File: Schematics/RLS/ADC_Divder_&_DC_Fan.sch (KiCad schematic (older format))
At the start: 11 parts, among them J7 DC_Fan, Q1 BS170

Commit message: Lots of changes
Completed Schematic
1/3 Done PCB
Multisim file for testing ADC protection and buffer circuit
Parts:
- added R34, R35, R36, R37: 10K, Resistors_SMD:R_1206_HandSoldering, symbol R
- added R38, R39: 1K, Resistors_SMD:R_1206_HandSoldering, symbol R
- added U15, U16, U19, U20: RB496EATR, TO_SOT_Packages_SMD:SOT-23-5_HandSoldering, symbol RB496EATR
- added U17, U18, U21: NE5532, Housings_SOIC:SOIC-8_3.9x4.9mm_Pitch1.27mm, symbol NE5532
- R11: value 20K -> 120
- R12: value 10K -> 120
- R13: value 20K -> 1K
- R14: value 10K -> 1K
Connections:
- net AGND: now also R34.1, R37.1, U15.5, U16.3, U18.5 (+), U19.3, U20.5, U21.5 (+); no longer R12.2, R14.2, R16.2
- net VM01: now also R15.2; no longer R15.1
- net VM02: now also R11.2; no longer R13.1
- net VM03: now also R35.2; no longer R11.1
- net FAN_GND: now reaches C45.2, J7.1 (P1), Q1.1 (D)
- net VGS_FAN: now reaches Q1.2 (G), R29.1, TH1.2
- net VD01 renamed +15_DIV
- net +15_DIV: now also R34.2, U17.5 (+); no longer R15.2
- net VD02 renamed -5_BUFF
- net -5_BUFF: now also U18.1, U18.2 (-); no longer R14.1
- net VD03 renamed +5_OVP
- net +5_OVP: now also U16.1, U16.4, U17.3 (+); no longer R11.2
- new net +15V: U17.8 (V+), U17.8 (V+), U18.8 (V+), U18.8 (V+), U19.5, U21.8 (V+), U21.8 (V+)
- new net +15_OVP: R15.1, R16.2, U19.1, U19.4
- new net +5V_R: U16.5
- new net -15V: U17.4 (V-), U17.4 (V-), U18.4 (V-), U18.4 (V-), U20.3, U21.4 (V-), U21.4 (V-)
- new net -15_BUFF: R38.2, U21.1, U21.2 (-)
- new net -15_DIV: R36.1, R37.2, U21.3 (+)
- new net -15_INV: R38.1, R39.2, U21.6 (-)
- new net -15_OVP: R35.1, R36.2, U20.1, U20.4
- new net -5V_R: U15.3
- new net -5_INV: R13.1, R14.2, U18.6 (-)
- new net -5_OVP: R11.1, U15.1, U15.4, U18.3 (+)
- new net AIN0: U17.1, U17.2 (-)
- new net AIN1: U17.6 (-), U17.7
- new net AIN2: R14.1, U18.7
- new net AIN3: R39.1, U21.7
- new net VM00: R12.2
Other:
- note added: "+15V Buffer Circuit"
- note added: "+5V Buffer Circuit"
- note added: "-15V Buffer and Inverting Circuit"
- note added: "-5V Buffer and Inverting Circuit"
- note added: "5V DC Fan with Thermal\nVoltage Control Circuit"
- moved on the sheet: C45, J7, Q1, R29, TH1

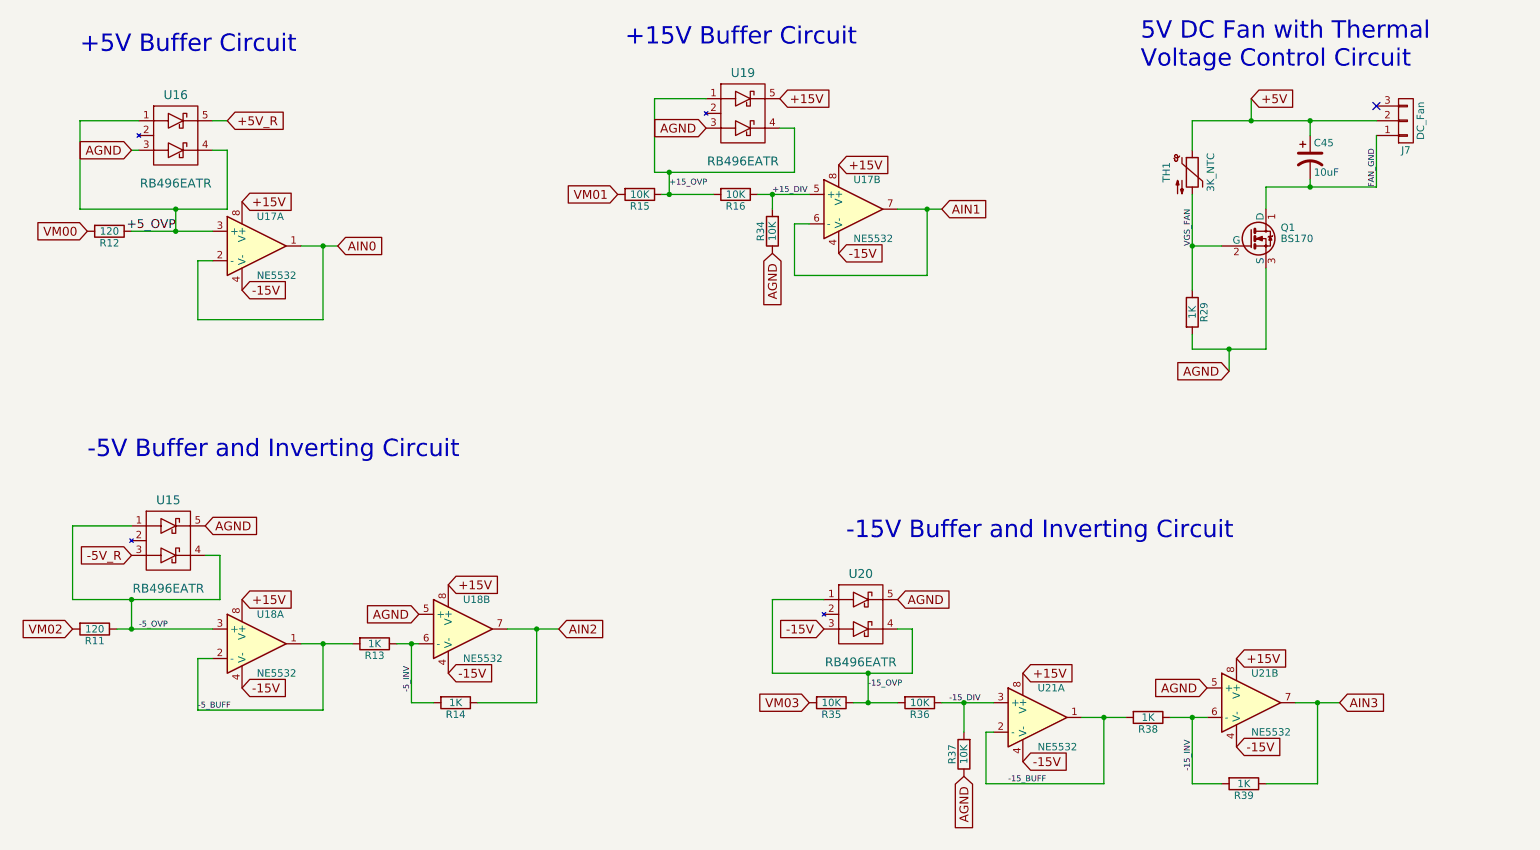
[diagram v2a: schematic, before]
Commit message: Finished PCB but...
Somehow managed to break the schematic file. I know how to fix it, but it is tedious and pointless for now (one has to go through every single individual component and verify that it is the same in the PCB, since the annotation script fucked everything up in the schematic, and therefore any new Netlist).
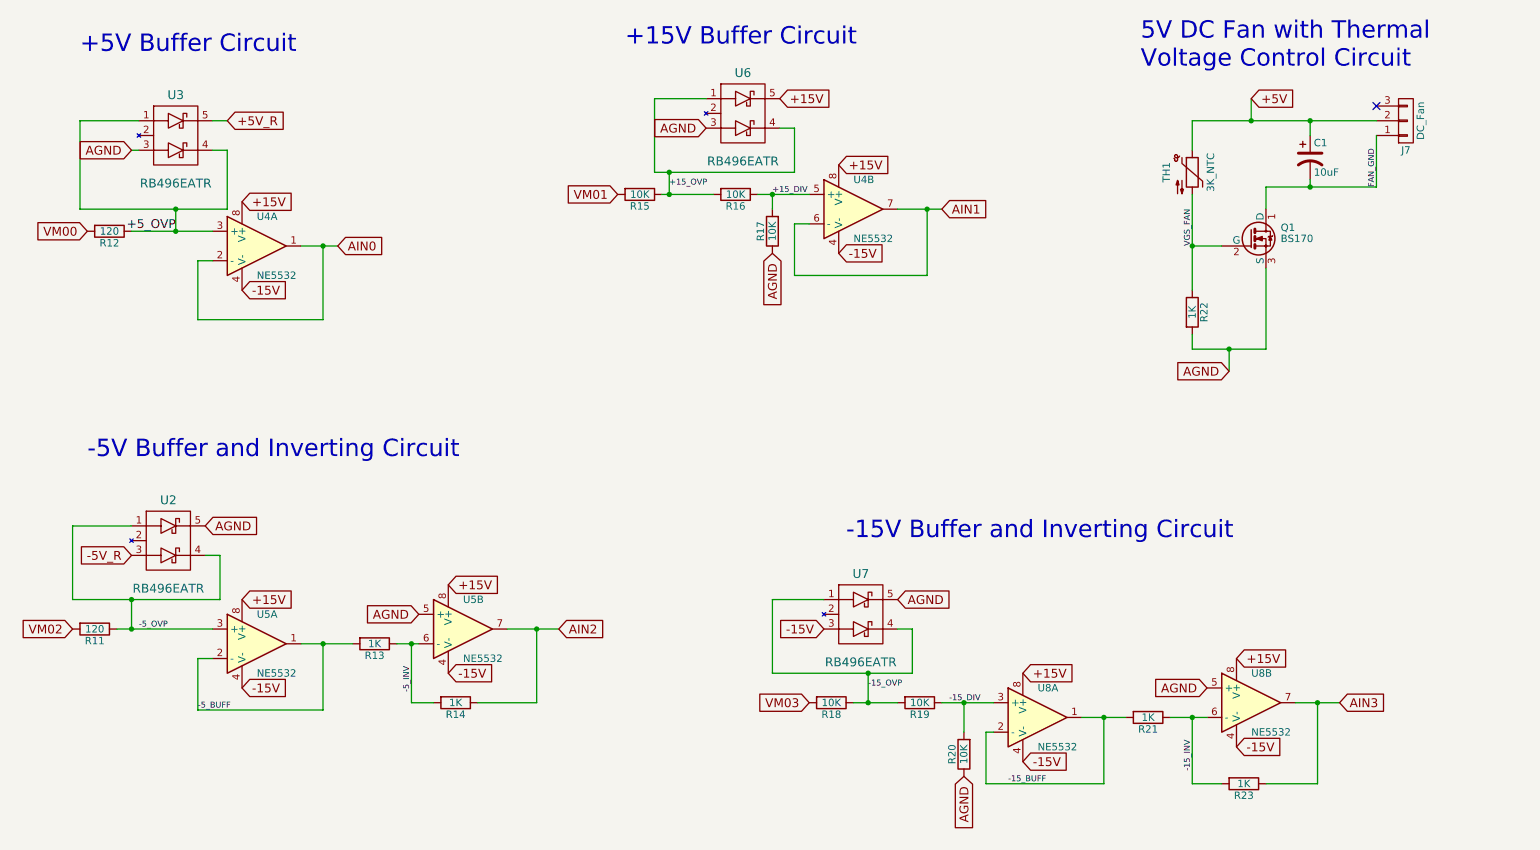
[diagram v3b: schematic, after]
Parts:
- renumbered C45 to C1, R34 to R17, R35 to R18, R36 to R19, R37 to R20, R38 to R21, R29 to R22, R39 to R23, U15 to U2, U16 to U3, U17 to U4, U18 to U5, U19 to U6, U20 to U7, U21 to U8
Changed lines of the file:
@@
 $EndComp
 $Comp
-L R R29
+L R R22
 U 1 1 595B0B7F
 P 8900 2650
-F 0 "R29" V 8980 2650 50  0000 C CNN
+F 0 "R22" V 8980 2650 50  0000 C CNN
 F 1 "1K" V 8900 2650 50  0000 C CNN
 F 2 "Resistors_SMD:R_1206_HandSoldering" V 8830 2650 50  0001 C CNN
@@
 $EndComp
 $Comp
-L CP1 C45
+L CP1 C1
 U 1 1 595B0C17
 P 9700 1600
-F 0 "C45" H 9725 1700 50  0000 L CNN
+F 0 "C1" H 9725 1700 50  0000 L CNN
 F 1 "10uF" H 9725 1500 50  0000 L CNN
 F 2 "Capacitors_SMD:CP_Elec_4x5.3" H 9700 1600 50  0001 C CNN
@@
 NoConn ~ 10150 1250
 $Comp
-L NE5532 U17
+L NE5532 U4
 U 1 1 59630AD8
 P 2550 2200
-F 0 "U17" H 2550 2400 50  0000 L CNN
+F 0 "U4" H 2550 2400 50  0000 L CNN
 F 1 "NE5532" H 2550 2000 50  0000 L CNN
 F 2 "Housings_SOIC:SOIC-8_3.9x4.9mm_Pitch1.27mm" H 2550 2200 50  0001 C CNN
@@
 $EndComp
 $Comp
-L NE5532 U17
+L NE5532 U4
 U 2 1 59630C05
 P 6600 1950
-F 0 "U17" H 6600 2150 50  0000 L CNN
+F 0 "U4" H 6600 2150 50  0000 L CNN
 F 1 "NE5532" H 6600 1750 50  0000 L CNN
 F 2 "Housings_SOIC:SOIC-8_3.9x4.9mm_Pitch1.27mm" H 6600 1950 50  0001 C CNN
@@
 $EndComp
 $Comp
-L NE5532 U18
+L NE5532 U5
 U 2 1 59630DE7
 P 3950 4800
-F 0 "U18" H 3950 5000 50  0000 L CNN
+F 0 "U5" H 3950 5000 50  0000 L CNN
 F 1 "NE5532" H 3950 4600 50  0000 L CNN
 F 2 "Housings_SOIC:SOIC-8_3.9x4.9mm_Pitch1.27mm" H 3950 4800 50  0001 C CNN
@@
 $EndComp
 $Comp
-L NE5532 U21
+L NE5532 U8
 U 1 1 59630E33
 P 7850 5400
-F 0 "U21" H 7850 5600 50  0000 L CNN
+F 0 "U8" H 7850 5600 50  0000 L CNN
 F 1 "NE5532" H 7850 5200 50  0000 L CNN
 F 2 "Housings_SOIC:SOIC-8_3.9x4.9mm_Pitch1.27mm" H 7850 5400 50  0001 C CNN
@@
 $EndComp
 $Comp
-L NE5532 U18
+L NE5532 U5
 U 1 1 59630FE7
 P 2550 4900
-F 0 "U18" H 2550 5100 50  0000 L CNN
+F 0 "U5" H 2550 5100 50  0000 L CNN
 F 1 "NE5532" H 2550 4700 50  0000 L CNN
 F 2 "Housings_SOIC:SOIC-8_3.9x4.9mm_Pitch1.27mm" H 2550 4900 50  0001 C CNN
@@
 $EndComp
 $Comp
-L NE5532 U21
+L NE5532 U8
 U 2 1 596310A4
 P 9300 5300
-F 0 "U21" H 9300 5500 50  0000 L CNN
+F 0 "U8" H 9300 5500 50  0000 L CNN
 F 1 "NE5532" H 9300 5100 50  0000 L CNN
 F 2 "Housings_SOIC:SOIC-8_3.9x4.9mm_Pitch1.27mm" H 9300 5300 50  0001 C CNN
@@
 $EndComp
 $Comp
-L RB496EATR U16
+L RB496EATR U3
 U 1 1 59631B31
 P 2000 1250
-F 0 "U16" H 2000 1325 60  0000 C CNN
+F 0 "U3" H 2000 1325 60  0000 C CNN
 F 1 "RB496EATR" H 2000 725 60  0000 C CNN
 F 2 "TO_SOT_Packages_SMD:SOT-23-5_HandSoldering" H 2000 1250 60  0001 C CNN
@@
 $EndComp
 $Comp
-L RB496EATR U19
+L RB496EATR U6
 U 1 1 59631C99
 P 5850 1100
-F 0 "U19" H 5850 1175 60  0000 C CNN
+F 0 "U6" H 5850 1175 60  0000 C CNN
 F 1 "RB496EATR" H 5850 575 60  0000 C CNN
 F 2 "TO_SOT_Packages_SMD:SOT-23-5_HandSoldering" H 5850 1100 60  0001 C CNN
@@
 $EndComp
 $Comp
-L RB496EATR U15
+L RB496EATR U2
 U 1 1 59631CCA
 P 1950 4000
-F 0 "U15" H 1950 4075 60  0000 C CNN
+F 0 "U2" H 1950 4075 60  0000 C CNN
 F 1 "RB496EATR" H 1950 3475 60  0000 C CNN
 F 2 "TO_SOT_Packages_SMD:SOT-23-5_HandSoldering" H 1950 4000 60  0001 C CNN
@@
 $EndComp
 $Comp
-L RB496EATR U20
+L RB496EATR U7
 U 1 1 59631D11
 P 6650 4500
-F 0 "U20" H 6650 4575 60  0000 C CNN
+F 0 "U7" H 6650 4575 60  0000 C CNN
 F 1 "RB496EATR" H 6650 3975 60  0000 C CNN
 F 2 "TO_SOT_Packages_SMD:SOT-23-5_HandSoldering" H 6650 4500 60  0001 C CNN
@@
 VM03
 $Comp
-L R R35
+L R R18
 U 1 1 5963265D
 P 6450 5300
-F 0 "R35" V 6530 5300 50  0000 C CNN
+F 0 "R18" V 6530 5300 50  0000 C CNN
 F 1 "10K" V 6450 5300 50  0000 C CNN
 F 2 "Resistors_SMD:R_1206_HandSoldering" V 6380 5300 50  0001 C CNN
@@
 $EndComp
 $Comp
-L R R34
+L R R17
 U 1 1 5962F8AF
 P 6050 2100
-F 0 "R34" V 6130 2100 50  0000 C CNN
+F 0 "R17" V 6130 2100 50  0000 C CNN
 F 1 "10K" V 6050 2100 50  0000 C CNN
 F 2 "Resistors_SMD:R_1206_HandSoldering" V 5980 2100 50  0001 C CNN
@@
 	8150 5400 8450 5400
 $Comp
-L R R38
+L R R21
 U 1 1 59635907
 P 8600 5400
-F 0 "R38" V 8680 5400 50  0000 C CNN
+F 0 "R21" V 8680 5400 50  0000 C CNN
 F 1 "1K" V 8600 5400 50  0000 C CNN
 F 2 "Resistors_SMD:R_1206_HandSoldering" V 8530 5400 50  0001 C CNN
@@
 Connection ~ 8300 5400
 $Comp
-L R R39
+L R R23
 U 1 1 59635A67
 P 9250 5850
-F 0 "R39" V 9330 5850 50  0000 C CNN
+F 0 "R23" V 9330 5850 50  0000 C CNN
 F 1 "1K" V 9250 5850 50  0000 C CNN
 F 2 "Resistors_SMD:R_1206_HandSoldering" V 9180 5850 50  0001 C CNN
@@
 Connection ~ 9750 5300
 $Comp
-L R R36
+L R R19
 U 1 1 59635DCB
 P 7050 5300
-F 0 "R36" V 7130 5300 50  0000 C CNN
+F 0 "R19" V 7130 5300 50  0000 C CNN
 F 1 "10K" V 7050 5300 50  0000 C CNN
 F 2 "Resistors_SMD:R_1206_HandSoldering" V 6980 5300 50  0001 C CNN
@@
 $EndComp
 $Comp
-L R R37
+L R R20
 U 1 1 59635F7D
 P 7350 5650
-F 0 "R37" V 7430 5650 50  0000 C CNN
+F 0 "R20" V 7430 5650 50  0000 C CNN
 F 1 "10K" V 7350 5650 50  0000 C CNN
 F 2 "Resistors_SMD:R_1206_HandSoldering" V 7280 5650 50  0001 C CNN

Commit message: Added Things and Fixed Schematic
Added pots to schematic and pcb for adc balancing.
Fixed the component annotation and netlist in the pcb.
Shrunk the pcb down a bit.
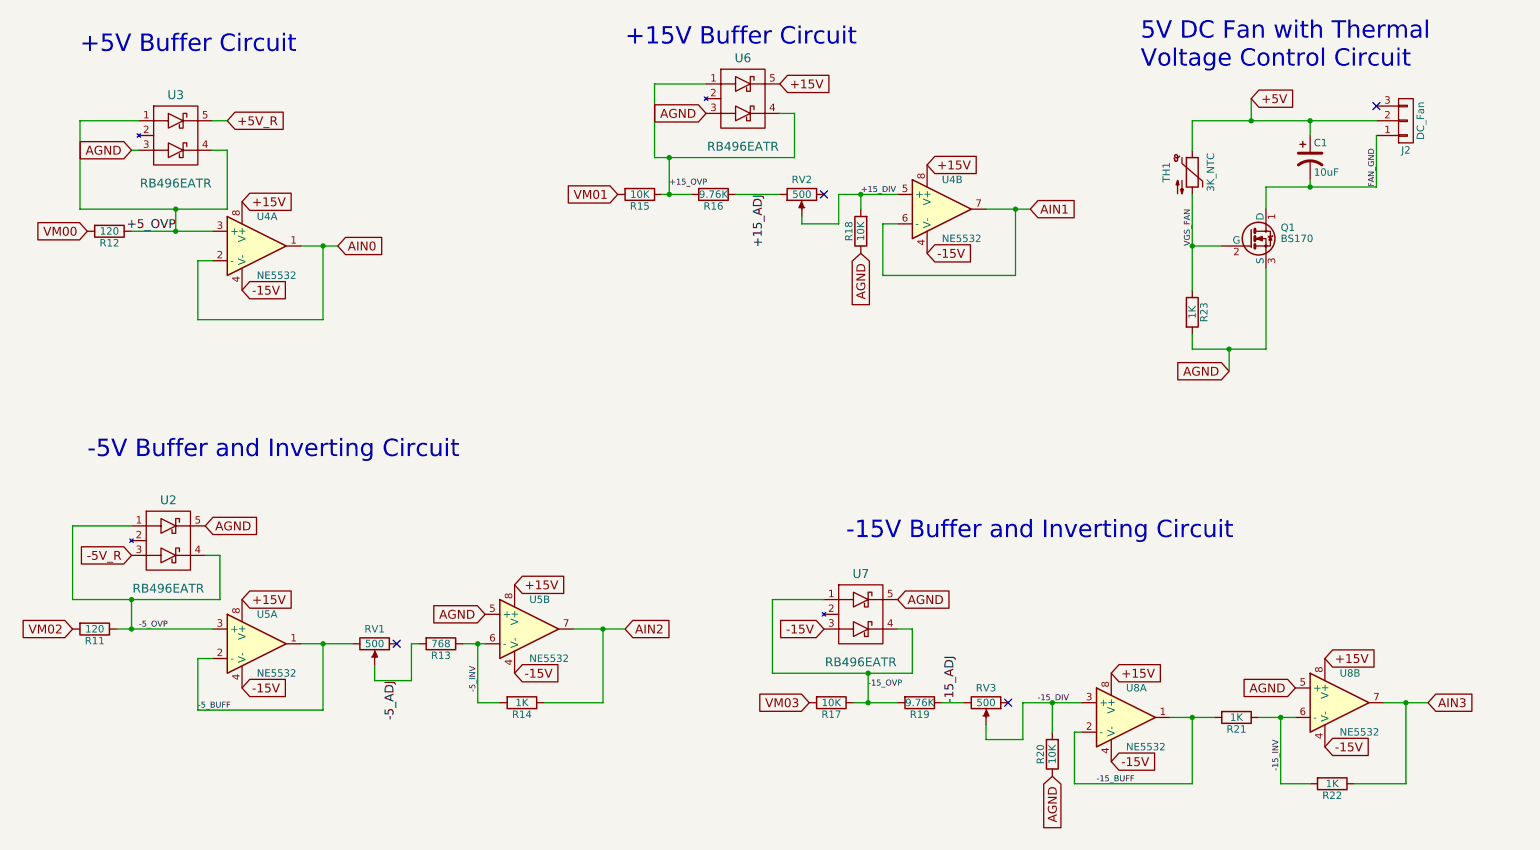
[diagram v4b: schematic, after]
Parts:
- added RV1, RV2, RV3: 500, RLS_CustomFootprints:Potentiometer_Trimmer_Bourns_PVG5A, symbol POT
- R13: value 1K -> 768
- R16, R19: value 10K -> 9.76K
- renumbered J7 to J2, R18 to R17, R17 to R18, R23 to R22, R22 to R23
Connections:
- net +15_DIV: now also RV2.2; no longer R16.1
- net -15_DIV: now also RV3.2; no longer R19.1
- net -5_BUFF: now also RV1.3; no longer R13.2
- new net +15_ADJ: R16.1, RV2.1
- new net -15_ADJ: R19.1, RV3.3
- new net -5_ADJ: R13.2, RV1.2
- no-connect marks 1 -> 4
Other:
- moved on the sheet: R13, R14, R16, R18, R20, R21, R22, U4B, U5B, U6, U8A, U8B
